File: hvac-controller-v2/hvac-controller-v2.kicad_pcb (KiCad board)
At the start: 2 copper layers, 50 x 30 mm, 48 parts, among them J1 VAC IN, J2 Conn_01x06, J3 UART, U1 ESP32-C3-MINI-1, U2 LM324DT, U3 TPS5430DDA, U4 TPS5430DDA

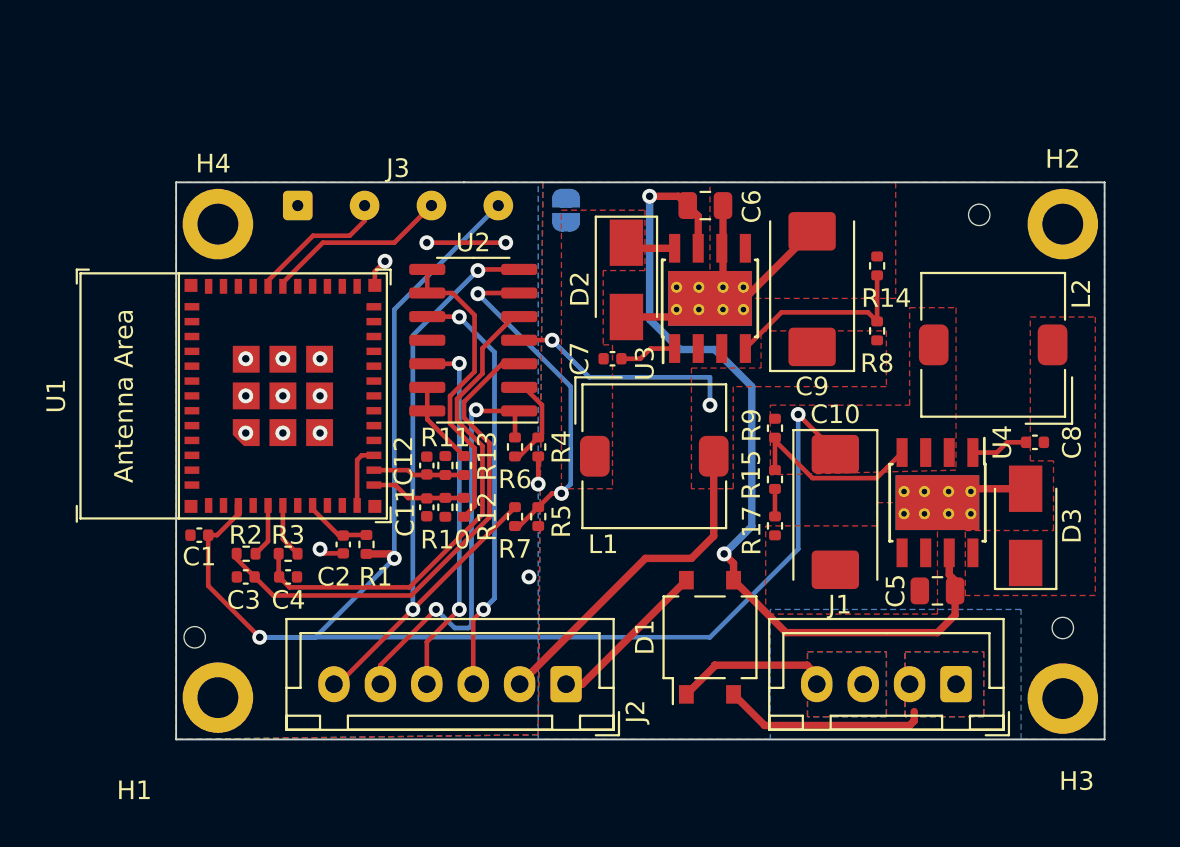
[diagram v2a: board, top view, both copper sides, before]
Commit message: Re-layout schematic and PCB
I wanted the antenna on top (long edge).
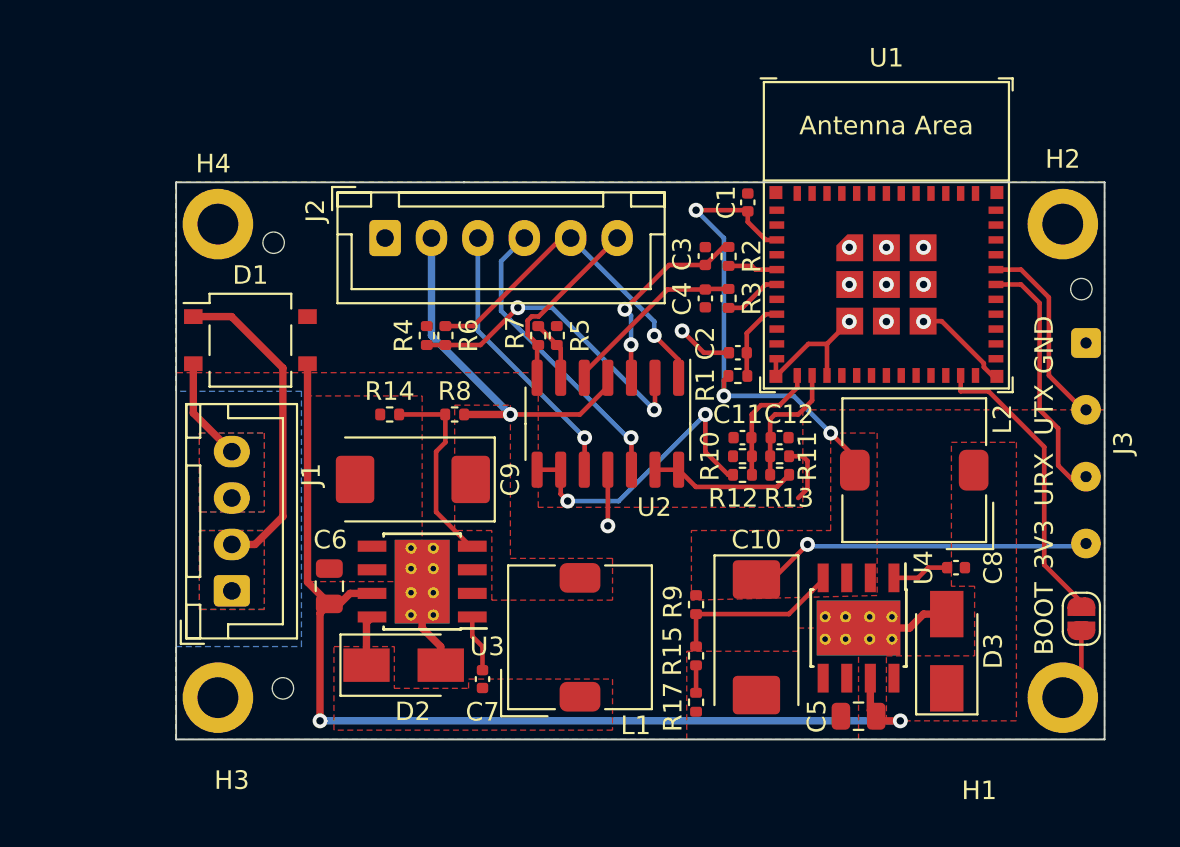
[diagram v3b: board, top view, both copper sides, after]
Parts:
- C1: value 0.01uF -> 0.01uF/16V
- C11, C12: value 0.1uF -> 0.1uF/16V
- JP1: moved to F.Cu
- moved H7 47.3 mm to (88.2, 89.8), turned to 180 degrees
- moved H3 45.5 mm to (85.2, 114.2)
- moved H1 45.5 mm to (130.8, 114.2)
- moved J3 43.1 mm to (132.0, 95.2), turned to -90 degrees
- moved J1 39.3 mm to (86.0, 108.5), turned to 90 degrees
- moved JP1 35.4 mm to (131.8, 110.0)
- moved C1 34.5 mm to (113.8, 87.6), turned to 90 degrees
- moved U1 33.0 mm to (121.2, 92.0), turned to 0 degrees
- moved R2 30.5 mm to (112.8, 90.5), turned to -90 degrees
- moved C3 30.2 mm to (111.5, 90.5), turned to 90 degrees
- moved D1 29.5 mm to (87.0, 95.0), turned to 0 degrees
- moved C6 28.8 mm to (91.2, 108.2), turned to 90 degrees
- moved R14 27.4 mm to (94.5, 99.0), turned to 0 degrees
- moved R3 27.4 mm to (112.8, 92.8), turned to -90 degrees
- moved C4 27.0 mm to (111.5, 92.8), turned to -90 degrees
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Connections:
- J1 pad 1: +24VA -> -24VA
- J1 pad 2: +24VA -> -24VA
- J1 pad 3: -24VA -> +24VA
- J1 pad 4: -24VA -> +24VA
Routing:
- net +3V3: track 82.3 -> 44.8 mm, vias 3 -> 4
- net /CTRL2_OUT: track 35.4 -> 10.0 mm, vias 2 -> 0
- net Net-(C4-Pad1): track 26.8 -> 9.91 mm
- net Net-(C3-Pad1): track 27.1 -> 10.8 mm, vias 0 -> 2
- net /BOOT: track 0.00 -> 16.1 mm
- net Net-(R5-Pad1): track 18.3 -> 3.29 mm, vias 2 -> 0
- net Net-(R4-Pad1): track 5.12 -> 17.1 mm, vias 0 -> 2
- net /D1_OUT: track 46.6 -> 57.3 mm
- net -24VA: track 8.63 -> 17.3 mm
- net +12V: track 30.7 -> 22.6 mm, vias 2 -> 1
- net /CTRL1_IN: track 22.8 -> 14.9 mm, vias 2 -> 1
- net GND: track 42.2 -> 35.1 mm, vias 15 -> 11
- net +24VA: track 11.0 -> 5.59 mm
- net /CTRL1_OUT: track 23.2 -> 18.9 mm, vias 2 -> 1
- net /UART_RX: track 9.92 -> 13.7 mm
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
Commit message: Update hvac controller with better clearances
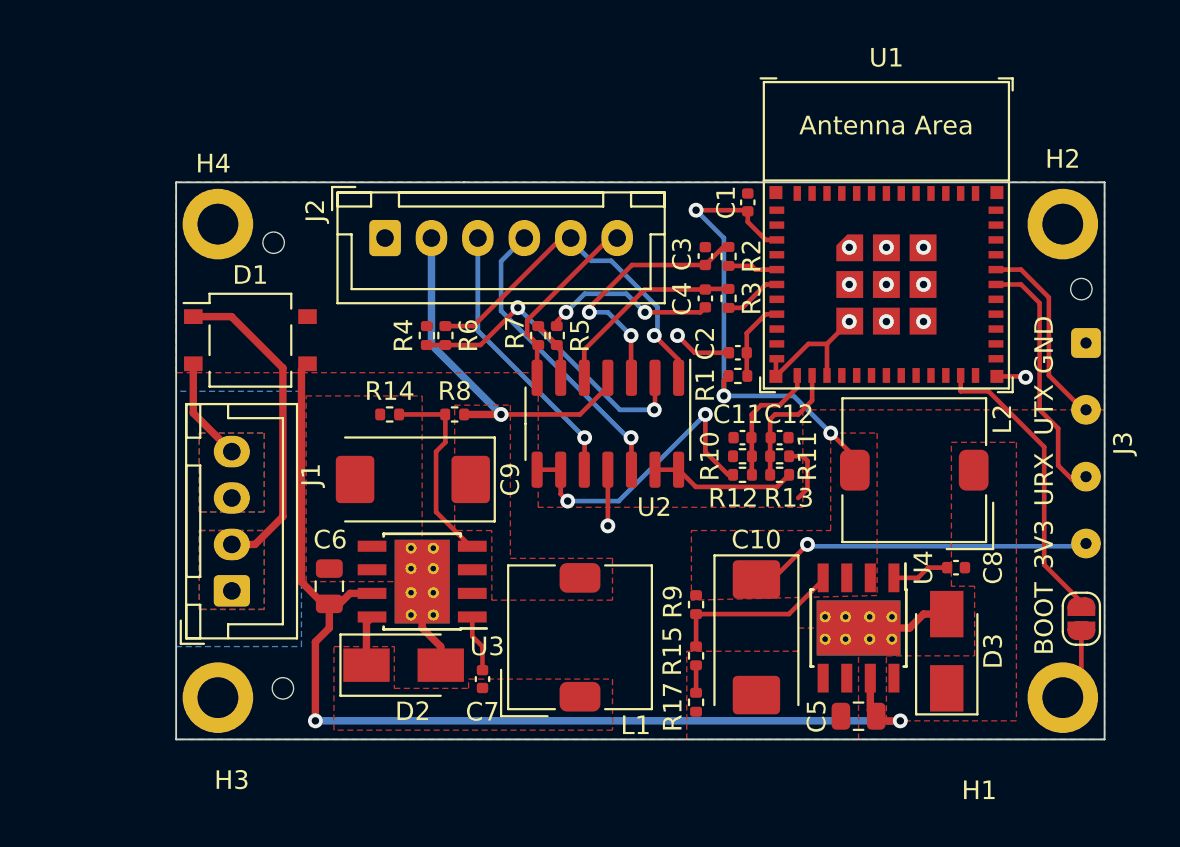
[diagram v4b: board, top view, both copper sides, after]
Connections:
- net /BOOT renamed Net-(JP1-Pad1)
- net /CHIP_PU renamed Net-(C2-Pad1)
- net /D1_OUT renamed Net-(C5-Pad1)
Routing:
- net GND: track 35.1 -> 40.9 mm, vias 11 -> 14
- net Net-(C3-Pad1): track 10.8 -> 14.2 mm
- net Net-(C5-Pad1): track 57.3 -> 58.1 mm
- net /CTRL1_OUT: track 18.9 -> 19.6 mm
- net Net-(C4-Pad1): track 9.91 -> 10.6 mm
- net +12V: track 22.6 -> 21.9 mm
